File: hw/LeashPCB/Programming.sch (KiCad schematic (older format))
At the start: 4 parts, among them J401 TAG-CONNECT-10, J402 Conn_ARM_JTAG_SWD_10

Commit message: Swapped out USB and antenna sections and refactored outline, started routing
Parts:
- removed C401: 0.1 uF, Capacitor_SMD:C_0402_1005Metric, symbol Device:C
- removed J402: Conn_ARM_JTAG_SWD_10, Connector_PinHeader_1.27mm:PinHeader_2x05_P1.27mm_Vertical_SMD, symbol Connector:Conn_ARM_JTAG_SWD_10
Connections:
- wire segments 29 -> 14
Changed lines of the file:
@@
 EESchema Schematic File Version 4
-LIBS:LeashPCB-cache
 EELAYER 30 0
 EELAYER END
 $Descr B 17000 11000
 encoding utf-8
-Sheet 4 10
+Sheet 3 9
 Title "BeagleDust Leash PCB"
 Date "2019-08-12"
@@
 Text HLabel 9625 5200 2    50   Input ~ 0
 ~RESET
-$Comp
-L Connector:Conn_ARM_JTAG_SWD_10 J402
-U 1 1 5D4EE33E
-P 8825 7025
-F 0 "J402" H 8382 7071 50  0000 R CNN
-F 1 "Conn_ARM_JTAG_SWD_10" H 8382 6980 50  0000 R CNN
-F 2 "Connector_PinHeader_1.27mm:PinHeader_2x05_P1.27mm_Vertical_SMD" H 8825 7025 50  0001 C CNN
-F 3 "http://infocenter.arm.com/help/topic/com.arm.doc.ddi0314h/DDI0314H_coresight_components_trm.pdf" V 8475 5775 50  0001 C CNN
-F 4 "CONN HEADER SMD 10POS 1.27MM" H 8825 7025 50  0001 C CNN "Description"
-F 5 "https://www.digikey.com/product-detail/en/sullins-connector-solutions/GRPB052VWQP-RC/S9013E-05-ND/1786428" H 8825 7025 50  0001 C CNN "Link1"
-F 6 "GRPB052VWQP-RC" H 8825 7025 50  0001 C CNN "MPN1"
-F 7 "-A1,-P" H 8825 7025 50  0001 C CNN "Population"
-F 8 "$0.52130" H 8825 7025 50  0001 C CNN "Standard Price"
-F 9 "Sullins Connector Solutions" H 8825 7025 50  0001 C CNN "Vendor1"
-F 10 "CONN HEADER SMD 10POS 1.27MM" H 8825 7025 50  0001 C CNN "Short Description"
-	1    8825 7025
-	1    0    0    -1
-$EndComp
-$Comp
-L Device:C C?
-U 1 1 5D4F1C98
-P 7375 6925
-AR Path="/5D4F1C98" Ref="C?"  Part="1"
-AR Path="/5D062DFA/5D4F1C98" Ref="C401"  Part="1"
-F 0 "C401" H 7490 6971 50  0000 L CNN
-F 1 "0.1 uF" H 7490 6880 50  0000 L CNN
-F 2 "Capacitor_SMD:C_0402_1005Metric" H 7413 6775 50  0001 C CNN
-F 3 "~" H 7375 6925 50  0001 C CNN
-F 4 "CAP CER 0.1UF 10V X5R 0402" H 7375 6925 50  0001 C CNN "Description"
-F 5 "https://www.digikey.com/product-detail/en/samsung-electro-mechanics/CL05A104MP5NNNC/1276-1443-1-ND/3889529" H 7375 6925 50  0001 C CNN "Link1"
-F 6 "CL05A104MP5NNNC" H 7375 6925 50  0001 C CNN "MPN1"
-F 7 "$0.00315" H 7375 6925 50  0001 C CNN "Standard Price"
-F 8 "Samsung Electro-Mechanics" H 7375 6925 50  0001 C CNN "Vendor1"
-F 9 "CAP CER 0.1UF 10V X5R 0402" H 7375 6925 50  0001 C CNN "Short Description"
-	1    7375 6925
-	1    0    0    -1
-$EndComp
-Wire Wire Line
-	7375 6400 7375 6775
-Connection ~ 7375 6400
-$Comp
-L power:+3V3 #PWR0155
-U 1 1 5D4F1CA5
-P 7375 6200
-F 0 "#PWR0155" H 7375 6050 50  0001 C CNN
-F 1 "+3V3" H 7390 6373 50  0000 C CNN
-F 2 "" H 7375 6200 50  0001 C CNN
-F 3 "" H 7375 6200 50  0001 C CNN
-	1    7375 6200
-	1    0    0    -1
-$EndComp
-Wire Wire Line
-	7375 6200 7375 6400
-Wire Wire Line
-	7375 7725 7375 7950
-$Comp
-L power:GND #PWR?
-U 1 1 5D4F1CB1
-P 7375 7950
-AR Path="/5D4F1CB1" Ref="#PWR?"  Part="1"
-AR Path="/5D062DFA/5D4F1CB1" Ref="#PWR0156"  Part="1"
-F 0 "#PWR0156" H 7375 7700 50  0001 C CNN
-F 1 "GND" H 7380 7777 50  0000 C CNN
-F 2 "" H 7375 7950 50  0001 C CNN
-F 3 "" H 7375 7950 50  0001 C CNN
-	1    7375 7950
-	-1   0    0    -1
-$EndComp
-Wire Wire Line
-	7375 7075 7375 7725
-Connection ~ 7375 7725
-Wire Wire Line
-	8825 6400 8825 6425
-Wire Wire Line
-	7375 6400 8825 6400
-Wire Wire Line
-	8825 7725 8825 7625
-Wire Wire Line
-	7375 7725 8725 7725
-Wire Wire Line
-	8725 7625 8725 7725
-Connection ~ 8725 7725
-Wire Wire Line
-	8725 7725 8825 7725
-Text HLabel 9875 7225 2    50   Input ~ 0
-TDI
-Text HLabel 9875 7125 2    50   Input ~ 0
-TDO
-Text HLabel 9875 6725 2    50   Input ~ 0
-~RESET
-Wire Wire Line
-	9325 6725 9875 6725
-Wire Wire Line
-	9325 7125 9875 7125
-Wire Wire Line
-	9875 7225 9325 7225
-Text HLabel 9900 6925 2    50   Input ~ 0
-TCK
-Wire Wire Line
-	9325 6925 9900 6925
-Text HLabel 9875 7025 2    50   Input ~ 0
-TMS
-Wire Wire Line
-	9325 7025 9875 7025
 Text HLabel 8225 5300 0    50   Input ~ 0
 TMS

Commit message: Migrated all hierarchical labels to global labels
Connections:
- net labels added: 3V3, CC1352_TCK, CC1352_TDI, CC1352_TDO, CC1352_TMS, RESET_N
- net labels removed: +3V3, TCK, TDI, TDO, TMS, ~RESET
- wire segments 14 -> 15
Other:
- moved on the sheet: C601
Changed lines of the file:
@@
 L Device:C C?
 U 1 1 5D08E161
-P 7600 5400
+P 7025 5400
 AR Path="/5D08E161" Ref="C?"  Part="1"
 AR Path="/5D062DFA/5D08E161" Ref="C601"  Part="1"
-F 0 "C601" H 7715 5446 50  0000 L CNN
-F 1 "0.1 uF" H 7715 5355 50  0000 L CNN
-F 2 "Capacitor_SMD:C_0402_1005Metric" H 7638 5250 50  0001 C CNN
-F 3 "~" H 7600 5400 50  0001 C CNN
-F 4 "CAP CER 0.1UF 10V X5R 0402" H 7600 5400 50  0001 C CNN "Description"
-F 5 "https://www.digikey.com/product-detail/en/samsung-electro-mechanics/CL05A104MP5NNNC/1276-1443-1-ND/3889529" H 7600 5400 50  0001 C CNN "Link1"
-F 6 "CL05A104MP5NNNC" H 7600 5400 50  0001 C CNN "MPN1"
-F 7 "$0.00315" H 7600 5400 50  0001 C CNN "Standard Price"
-F 8 "Samsung Electro-Mechanics" H 7600 5400 50  0001 C CNN "Vendor1"
-F 9 "CAP CER 0.1UF 10V X5R 0402" H 7600 5400 50  0001 C CNN "Short Description"
-F 10 "+A1" H 7600 5400 50  0001 C CNN "Population"
-	1    7600 5400
+F 0 "C601" H 7140 5446 50  0000 L CNN
+F 1 "0.1 uF" H 7140 5355 50  0000 L CNN
+F 2 "Capacitor_SMD:C_0402_1005Metric" H 7063 5250 50  0001 C CNN
+F 3 "~" H 7025 5400 50  0001 C CNN
+F 4 "CAP CER 0.1UF 10V X5R 0402" H 7025 5400 50  0001 C CNN "Description"
+F 5 "https://www.digikey.com/product-detail/en/samsung-electro-mechanics/CL05A104MP5NNNC/1276-1443-1-ND/3889529" H 7025 5400 50  0001 C CNN "Link1"
+F 6 "CL05A104MP5NNNC" H 7025 5400 50  0001 C CNN "MPN1"
+F 7 "$0.00315" H 7025 5400 50  0001 C CNN "Standard Price"
+F 8 "Samsung Electro-Mechanics" H 7025 5400 50  0001 C CNN "Vendor1"
+F 9 "CAP CER 0.1UF 10V X5R 0402" H 7025 5400 50  0001 C CNN "Short Description"
+F 10 "+A1" H 7025 5400 50  0001 C CNN "Population"
+	1    7025 5400
 	1    0    0    -1
 $EndComp
 Wire Wire Line
-	7600 5200 7600 5250
-Connection ~ 7600 5200
+	7025 5200 7025 5250
+Connection ~ 7025 5200
 Wire Wire Line
-	7600 5200 8625 5200
-Wire Wire Line
-	9125 5200 9625 5200
+	7025 5200 8625 5200
 Wire Wire Line
 	8625 5300 8225 5300
 Wire Wire Line
 	9125 5600 9625 5600
-$Comp
-L power:+3V3 #PWR0110
-U 1 1 5D46AF03
-P 7600 5000
-F 0 "#PWR0110" H 7600 4850 50  0001 C CNN
-F 1 "+3V3" H 7615 5173 50  0000 C CNN
-F 2 "" H 7600 5000 50  0001 C CNN
-F 3 "" H 7600 5000 50  0001 C CNN
-	1    7600 5000
-	1    0    0    -1
-$EndComp
-Wire Wire Line
-	7600 5000 7600 5200
 $Comp
 L Connector_Generic:Conn_02x05_Counter_Clockwise J401
@@
 	8625 5600 8500 5600
 Wire Wire Line
-	7600 5600 7600 5825
+	7025 5600 7025 5825
 $Comp
 L power:GND #PWR?
 U 1 1 5D4C51BB
-P 7600 5825
+P 7025 5825
 AR Path="/5D4C51BB" Ref="#PWR?"  Part="1"
 AR Path="/5D062DFA/5D4C51BB" Ref="#PWR0154"  Part="1"
-F 0 "#PWR0154" H 7600 5575 50  0001 C CNN
-F 1 "GND" H 7605 5652 50  0000 C CNN
-F 2 "" H 7600 5825 50  0001 C CNN
-F 3 "" H 7600 5825 50  0001 C CNN
-	1    7600 5825
+F 0 "#PWR0154" H 7025 5575 50  0001 C CNN
+F 1 "GND" H 7030 5652 50  0000 C CNN
+F 2 "" H 7025 5825 50  0001 C CNN
+F 3 "" H 7025 5825 50  0001 C CNN
+	1    7025 5825
 	-1   0    0    -1
 $EndComp
@@
 Connection ~ 8500 5600
 Wire Wire Line
-	8500 5600 7600 5600
+	8500 5600 7025 5600
 Wire Wire Line
-	7600 5550 7600 5600
-Connection ~ 7600 5600
+	7025 5550 7025 5600
+Connection ~ 7025 5600
 NoConn ~ 9125 5300
-Text HLabel 9625 5400 2    50   Input ~ 0
-TDI
-Text HLabel 9625 5600 2    50   Input ~ 0
-TDO
-Text HLabel 9625 5200 2    50   Input ~ 0
-~RESET
-Text HLabel 8225 5300 0    50   Input ~ 0
-TMS
-Text HLabel 8225 5500 0    50   Input ~ 0
-TCK
+Text GLabel 9625 5200 2    63   Input ~ 0
+RESET_N
+Text GLabel 9625 5400 2    63   Input ~ 0
+CC1352_TDI
+Text GLabel 8225 5300 0    63   Input ~ 0
+CC1352_TMS
+Text GLabel 8225 5500 0    63   Input ~ 0
+CC1352_TCK
+Wire Wire Line
+	9125 5200 9625 5200
+Text GLabel 9625 5600 2    63   Input ~ 0
+CC1352_TDO
+Text GLabel 6800 4950 0    63   Input ~ 0
+3V3
+Wire Wire Line
+	6800 4950 7025 4950
+Wire Wire Line
+	7025 4950 7025 5200
 $EndSCHEMATC

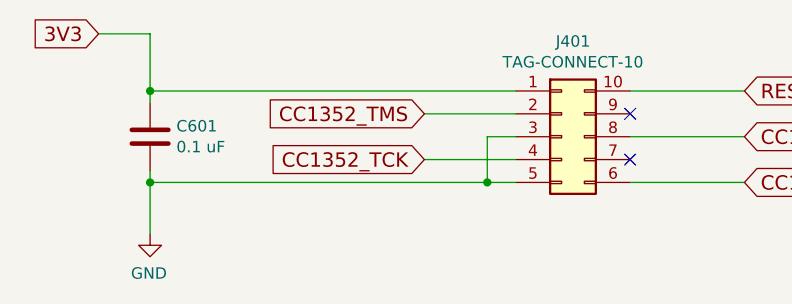
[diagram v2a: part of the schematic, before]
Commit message: Removed two extra pullup resistors
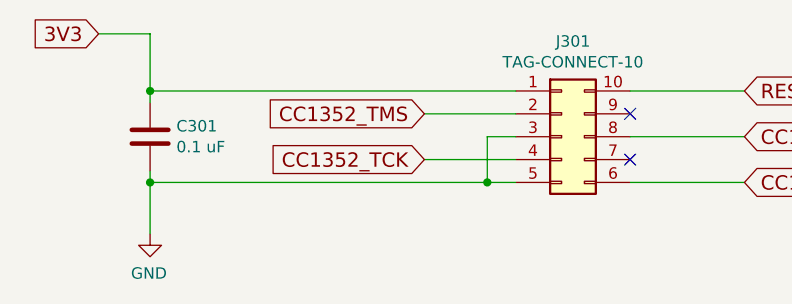
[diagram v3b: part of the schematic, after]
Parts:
- renumbered C601 to C301, J401 to J301
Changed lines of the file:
@@
 P 7025 5400
 AR Path="/5D08E161" Ref="C?"  Part="1"
-AR Path="/5D062DFA/5D08E161" Ref="C601"  Part="1"
-F 0 "C601" H 7140 5446 50  0000 L CNN
+AR Path="/5D062DFA/5D08E161" Ref="C301"  Part="1"
+F 0 "C301" H 7140 5446 50  0000 L CNN
 F 1 "0.1 uF" H 7140 5355 50  0000 L CNN
 F 2 "Capacitor_SMD:C_0402_1005Metric" H 7063 5250 50  0001 C CNN
@@
 	9125 5600 9625 5600
 $Comp
-L Connector_Generic:Conn_02x05_Counter_Clockwise J401
+L Connector_Generic:Conn_02x05_Counter_Clockwise J301
 U 1 1 5D471BC7
 P 8825 5400
-F 0 "J401" H 8875 5817 50  0000 C CNN
+F 0 "J301" H 8875 5817 50  0000 C CNN
 F 1 "TAG-CONNECT-10" H 8875 5726 50  0000 C CNN
 F 2 "leash:Tag-Connect-10" H 8825 5400 50  0001 C CNN
@@
 P 7025 5825
 AR Path="/5D4C51BB" Ref="#PWR?"  Part="1"
-AR Path="/5D062DFA/5D4C51BB" Ref="#PWR0154"  Part="1"
-F 0 "#PWR0154" H 7025 5575 50  0001 C CNN
+AR Path="/5D062DFA/5D4C51BB" Ref="#PWR0301"  Part="1"
+F 0 "#PWR0301" H 7025 5575 50  0001 C CNN
 F 1 "GND" H 7030 5652 50  0000 C CNN
 F 2 "" H 7025 5825 50  0001 C CNN

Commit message: Updated after latest Rev B build and BOM update, including new STEP file export
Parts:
- C301, J301: Population +A1 -> (none)
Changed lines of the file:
@@
 F 8 "Samsung Electro-Mechanics" H 7025 5400 50  0001 C CNN "Vendor1"
 F 9 "CAP CER 0.1UF 10V X5R 0402" H 7025 5400 50  0001 C CNN "Short Description"
-F 10 "+A1" H 7025 5400 50  0001 C CNN "Population"
+F 10 "" H 7025 5400 50  0001 C CNN "Population"
 	1    7025 5400
 	1    0    0    -1
@@
 F 5 "N/A" H 8825 5400 50  0001 C CNN "Link1"
 F 6 "N/A" H 8825 5400 50  0001 C CNN "MPN1"
-F 7 "+A1" H 8825 5400 50  0001 C CNN "Population"
+F 7 "" H 8825 5400 50  0001 C CNN "Population"
 F 8 "0" H 8825 5400 50  0001 C CNN "Standard Price"
 F 9 "Tag Connect, Inc" H 8825 5400 50  0001 C CNN "Vendor1"

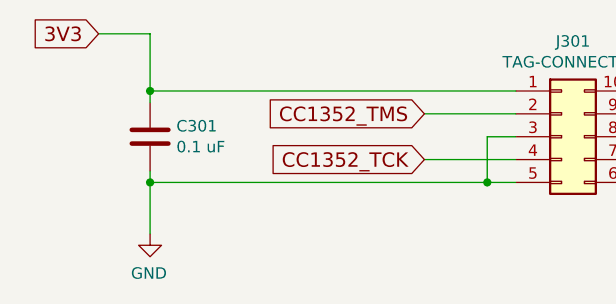
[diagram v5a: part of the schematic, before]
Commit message: Revisions and fixes for Rev B board in preparation for Rev C start. Changed how we handle the MSP430 and how it connects to the cc1352r. Also some part swaps and pin swaps on the cc1352r. Fixes #4 and #5.
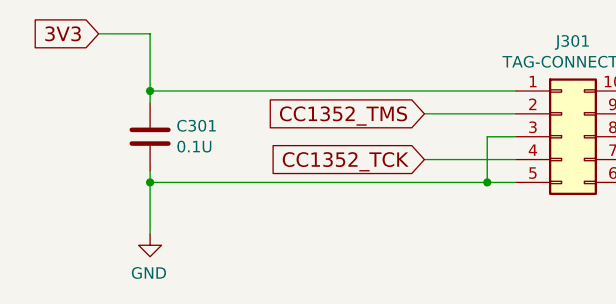
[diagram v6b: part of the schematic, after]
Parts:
- C301: value 0.1 uF -> 0.1U
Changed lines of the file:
@@
 AR Path="/5D062DFA/5D08E161" Ref="C301"  Part="1"
 F 0 "C301" H 7140 5446 50  0000 L CNN
-F 1 "0.1 uF" H 7140 5355 50  0000 L CNN
+F 1 "0.1U" H 7140 5355 50  0000 L CNN
 F 2 "Capacitor_SMD:C_0402_1005Metric" H 7063 5250 50  0001 C CNN
 F 3 "~" H 7025 5400 50  0001 C CNN
